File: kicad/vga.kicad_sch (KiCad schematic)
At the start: 19 parts, among them J2 DE15_Receptacle_HighDensity_M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, Q2 BC547, U17 74HC174, U18 XC9536PC44, U19 74HC574, U20 74HC574, U21 74HC245, U22 74HC02, U23 74HC138, U24 6264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

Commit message: Add user IO and USB
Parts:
- Q2: footprint Package_TO_SOT_THT_AKL:TO-92_Inline_Wide_CBE -> Package_TO_SOT_THT:TO-92
- U17: footprint Package_DIP:DIP-14_W7.62mm -> Package_DIP:DIP-16_W7.62mm
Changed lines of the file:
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@@
 			)
 		)
-		(property "Footprint" "Package_TO_SOT_THT_AKL:TO-92_Inline_Wide_CBE"
+		(property "Footprint" "Package_TO_SOT_THT:TO-92"
 			(at 270.51 88.9 0)
 			(effects
@@
 			)
 		)
-		(property "Footprint" "Package_DIP:DIP-14_W7.62mm"
+		(property "Footprint" "Package_DIP:DIP-16_W7.62mm"
 			(at 179.07 99.06 0)
 			(effects

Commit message: Add caps and make initial placement
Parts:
- added C26, C27, C28, C29, C30, C31, C32, C33, C34, C35, C36: 100n, Capacitor_THT:C_Disc_D5.0mm_W2.5mm_P2.50mm, symbol Device:C
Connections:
- net GND: now also C26.2, C27.2, C28.2, C29.2, C30.2, C31.2, C32.2, C33.2, C34.2, C35.2, C36.2
- net VCC: now also C26.1, C27.1, C28.1, C29.1, C30.1, C31.1, C32.1, C33.1, C34.1, C35.1, C36.1
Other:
- moved on the sheet: U22A

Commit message: Bugfixes, start routing
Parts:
- added U6: 74HC04, Package_DIP:DIP-14_W7.62mm, symbol 74xx:74HC04
- R15, R16, R17: value 330R -> 470R
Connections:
- net D6: no longer U20.8 (D6)
- net D7: no longer U19.9 (D7), U20.9 (D7)
- net GND: now also U19.9 (D7), U20.8 (D6), U20.9 (D7); no longer U22.2, U22.3, U23.6 (E2)
- net ROW3: now also U20.19 (Q0); no longer U19.12 (Q7)
- net ROW4: now also U20.18 (Q1); no longer U20.19 (Q0)
- net ROW5: now also U20.17 (Q2); no longer U20.18 (Q1)
- net ROW6: now also U20.16 (Q3); no longer U20.17 (Q2)
- net ROW7: now also U20.15 (Q4); no longer U20.16 (Q3)
- net ROW8: now also U20.14 (Q5); no longer U20.15 (Q4)
- net VCC: now also U23.6 (E2)
- net ~{BLANK}: now also U22.8; no longer U22.9
- net ~{WR}: now also U22.3; no longer U24.27 (~{WR})
- net at U22.11, U22.12: now also U19.1 (OE), U20.1 (OE), U21.19 (CE), U22.2, U23.15 (~{Y0}); no longer U24.22 (~{OE})
- net at U22.1: now also U24.22 (~{OE}), U6.13
- net at U27.13 (Qh): now also U22.9; no longer U22.8
- net at U20.13 (Q6): no longer U26.2 (A12)
- net ROMSEL0: now reaches U26.23 (A11)
- net ROMSEL0: no longer U20.14 (Q5)
- new net: U24.27 (~{WR}), U6.12
- new net ROMSEL1: U26.2 (A12)
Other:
- moved on the sheet: U22A, U22C

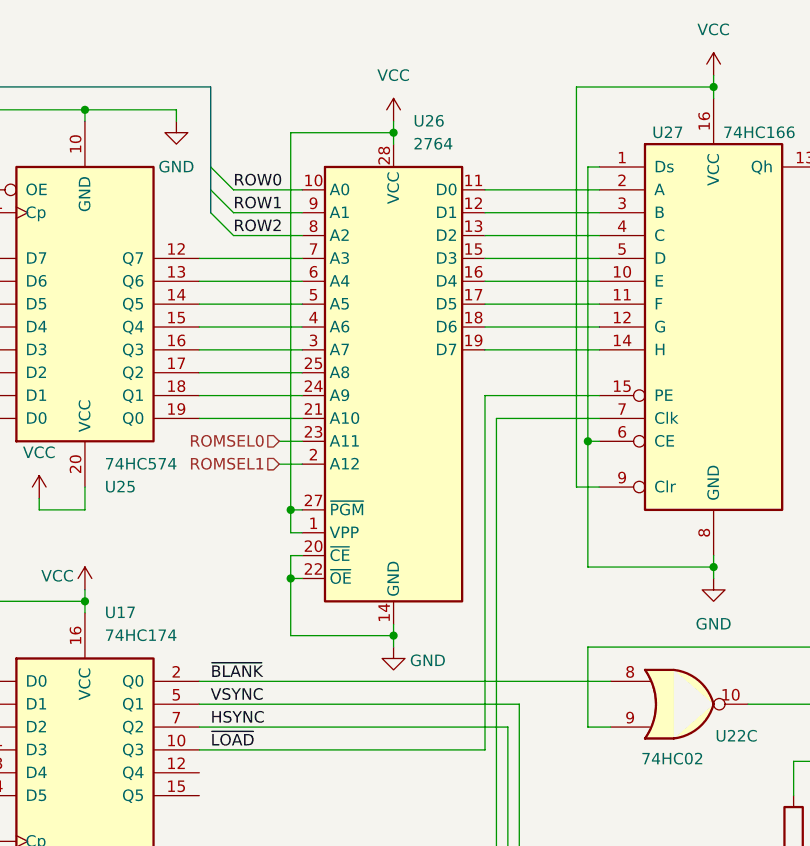
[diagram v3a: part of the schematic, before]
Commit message: Finished routing, HW prototype ready
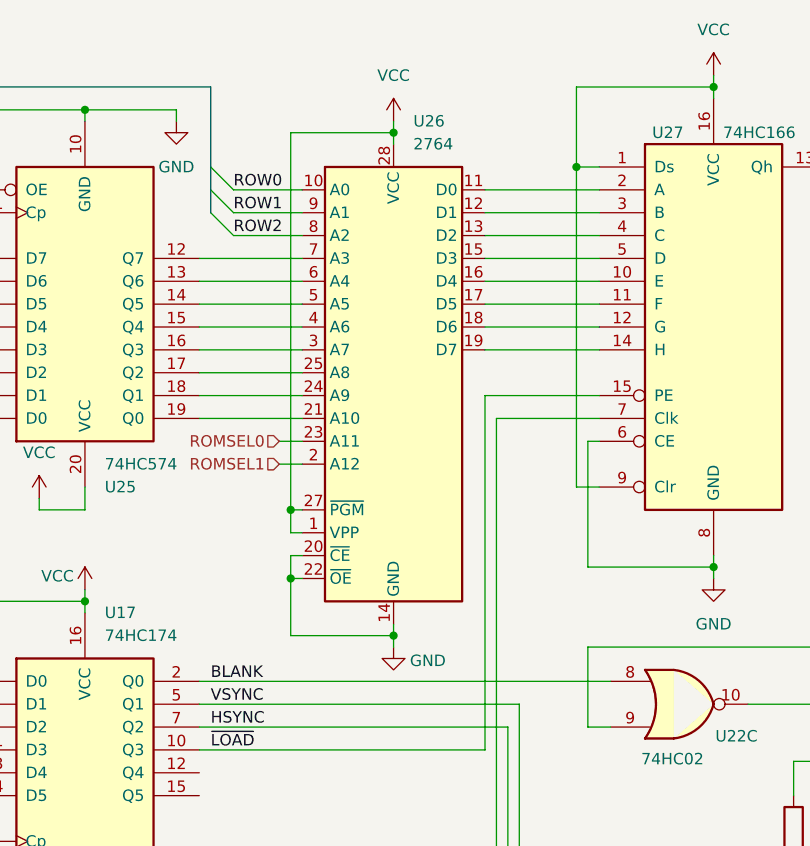
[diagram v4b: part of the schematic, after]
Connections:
- net GND: no longer U27.1 (Ds)
- net VCC: now also U27.1 (Ds)
- net ~{BLANK} renamed BLANK
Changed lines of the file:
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@@
 	)
 	(junction
+		(at 233.68 31.75)
+		(diameter 0)
+		(color 0 0 0 0)
+	)
+	(junction
 		(at 247.65 111.76)
 		(diameter 0)
@@
 	)
 	(junction
-		(at 234.95 62.23)
-		(diameter 0)
-		(color 0 0 0 0)
-	)
-	(junction
 		(at 163.83 125.73)
 		(diameter 0)
@@
 	(wire
 		(pts
-			(xy 233.68 22.86) (xy 233.68 67.31)
+			(xy 233.68 22.86) (xy 233.68 31.75)
 		)
 		(stroke
@@
 	(wire
 		(pts
+			(xy 233.68 31.75) (xy 233.68 67.31)
+		)
+		(stroke
+			(width 0)
+			(type default)
+		)
+	)
+	(wire
+		(pts
 			(xy 195.58 36.83) (xy 203.2 36.83)
 		)
@@
 	(wire
 		(pts
-			(xy 234.95 31.75) (xy 236.22 31.75)
+			(xy 233.68 31.75) (xy 236.22 31.75)
 		)
 		(stroke
@@
 	(wire
 		(pts
-			(xy 234.95 31.75) (xy 234.95 62.23)
-		)
-		(stroke
-			(width 0)
-			(type default)
-		)
-	)
-	(wire
-		(pts
 			(xy 71.12 144.78) (xy 74.93 144.78)
 		)
@@
 		)
 	)
-	(label "~{BLANK}"
+	(label "BLANK"
 		(at 193.04 88.9 0)
 		(fields_autoplaced yes)

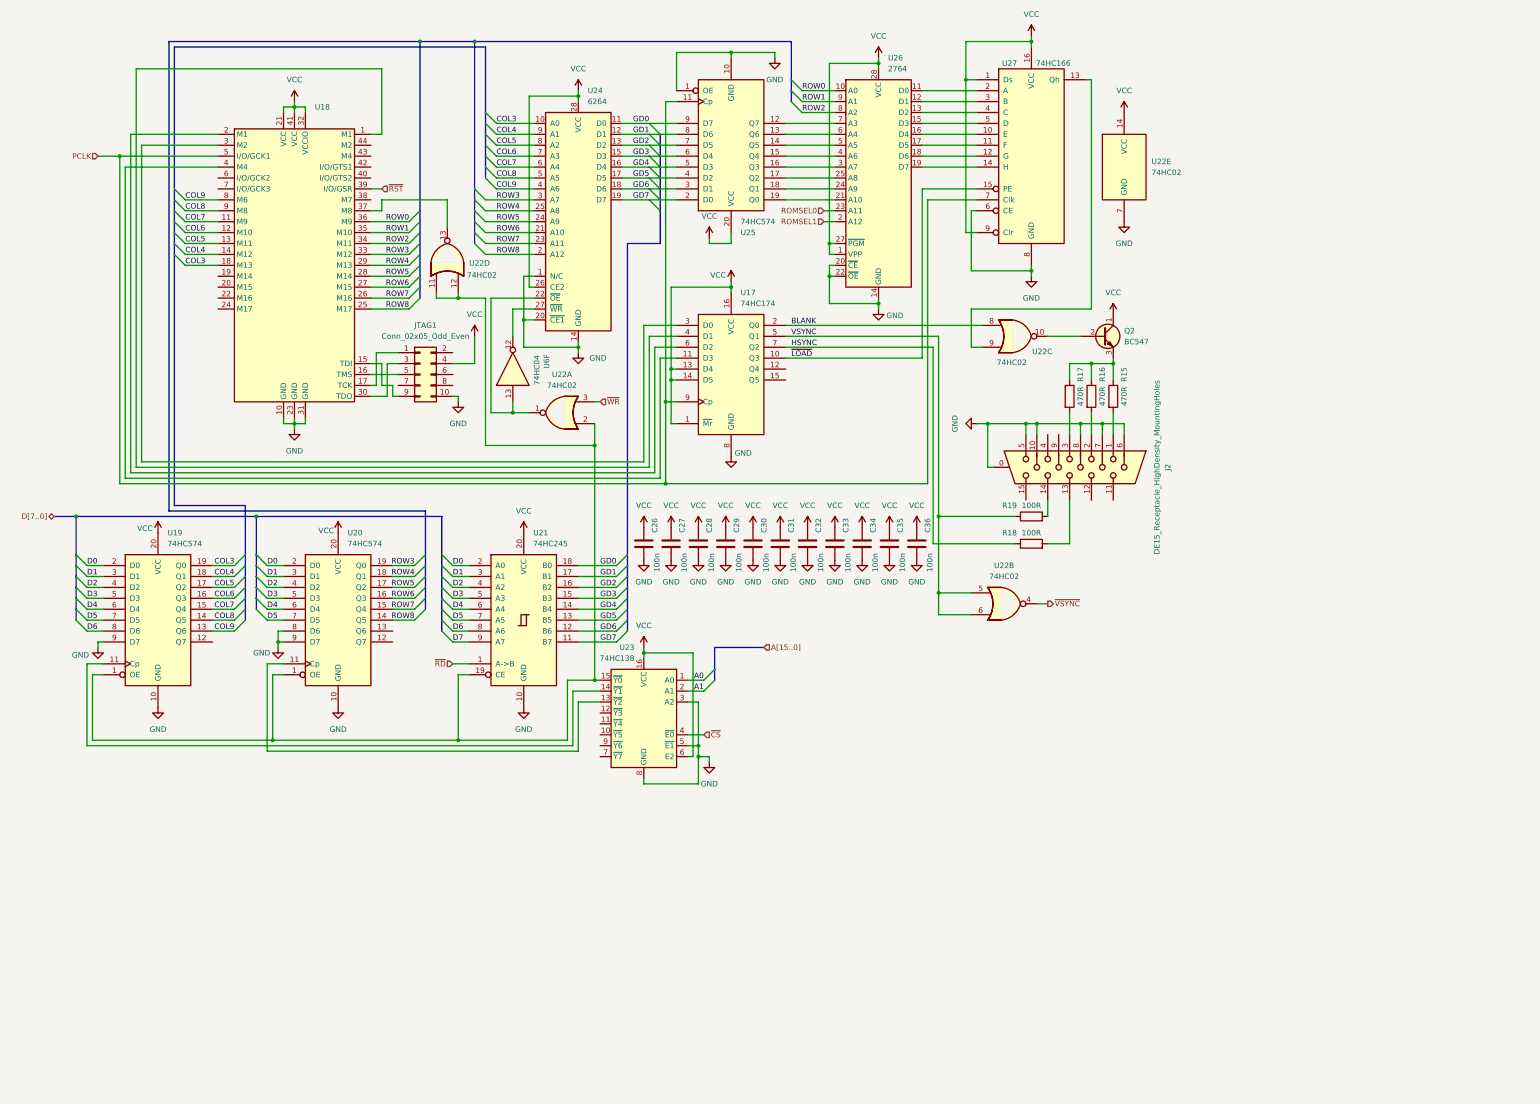
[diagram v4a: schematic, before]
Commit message: hw: Start work on rev B
Changelog:
- fixed IO address decoder (removed /PH2 gating),
- added missing reset circuit capacitor,
- added hardware VGA scrolling,
- removed VGA column register, replaced with address bus,
- fixed values of R5 and R6.
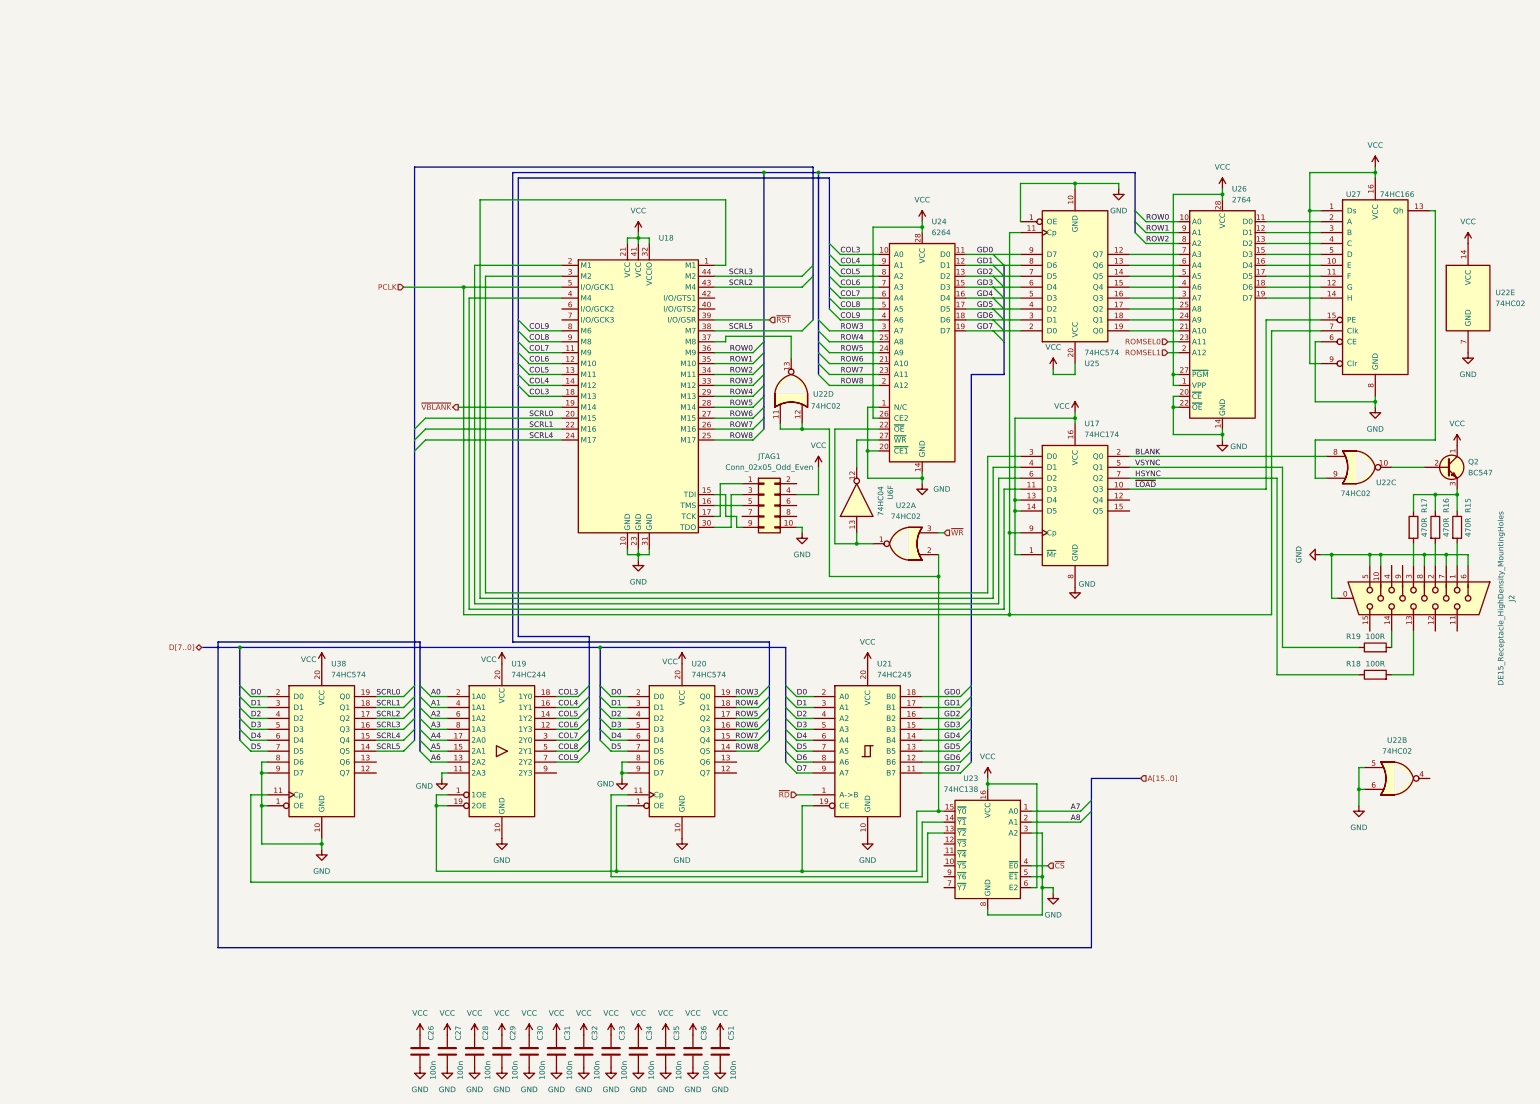
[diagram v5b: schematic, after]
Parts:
- removed U19: 74HC574, Package_DIP:DIP-20_W7.62mm, symbol 74xx:74HCT574
- added C51: 100n, Capacitor_THT:C_Disc_D5.0mm_W2.5mm_P2.50mm, symbol Device:C
- added U19: 74HC244, Package_DIP:DIP-20_W7.62mm, symbol 74xx:74HC244
- added U38: 74HC574, Package_DIP:DIP-20_W7.62mm, symbol 74xx:74HCT574
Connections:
- net A0: now also U19.2 (1A0); no longer U23.1 (A0)
- net A1: now also U19.4 (1A1); no longer U23.2 (A1)
- net COL3: now also U19.18 (1Y0)
- net COL4: now also U19.16 (1Y1)
- net COL5: now also U19.14 (1Y2)
- net COL6: now also U19.12 (1Y3)
- net COL7: now also U19.3 (2Y0)
- net COL8: now also U19.5 (2Y1)
- net COL9: now also U19.7 (2Y2)
- net D0: now also U38.2 (D0)
- net D1: now also U38.3 (D1)
- net D2: now also U38.4 (D2)
- net D3: now also U38.5 (D3)
- net D4: now also U38.6 (D4)
- net D5: now also U38.7 (D5)
- net GND: now also U22.5, U22.6, C51.2, U19.10 (GND), U19.11 (2A3), U38.1 (OE), U38.10 (GND), U38.8 (D6), U38.9 (D7)
- net VCC: now also C51.1, U19.20 (VCC), U38.20 (VCC)
- net VSYNC: no longer U22.5, U22.6
- net at U20.1 (OE), U21.19 (CE), U22.11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: now also U19.1 (1OE), U19.19 (2OE)
- net at U23.14 (~{Y1}): now also U20.11 (Cp)
- net at U23.13 (~{Y2}): now also U38.11 (Cp); no longer U20.11 (Cp)
- net ~{VBLANK}: now reaches U18.19 (M14)
- net SCRL0: now reaches U18.20 (M15)
- net SCRL0: now also U38.19 (Q0)
- net SCRL1: now reaches U18.22 (M16)
- net SCRL1: now also U38.18 (Q1)
- net SCRL4: now reaches U18.24 (M17)
- net SCRL4: now also U38.15 (Q4)
- net SCRL5: now reaches U18.38 (M7)
- net SCRL5: now also U38.14 (Q5)
- net SCRL2: now reaches U18.43 (M4)
- net SCRL2: now also U38.17 (Q2)
- net SCRL3: now reaches U18.44 (M2)
- net SCRL3: now also U38.16 (Q3)
- net ~{VSYNC}: no longer names the net of U22.4
- new net A2: U19.6 (1A2)
- new net A3: U19.8 (1A3)
- new net A4: U19.17 (2A0)
- new net A5: U19.15 (2A1)
- new net A6: U19.13 (2A2)
- new net A7: U23.1 (A0)
- new net A8: U23.2 (A1)
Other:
- moved on the sheet: C26, C27, C28, C29, C30, C31, C32, C33, C34, C35, C36, J2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

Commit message: hw: revision C
Major changes:
- ROM space has been extended from 16 KiB to 32 KiB
- dynamic RAM option has been removed
- RAM size has been reduced from 32 KiB to 24 KiB
- expansion slot now replaces internal ROM, does not
  have dedicated memory space anymore
- place all I/O within a compactish 8 KiB
- move PH2 gating to /RD and /WR signals
- PCB redo (mechanicaly compatible)
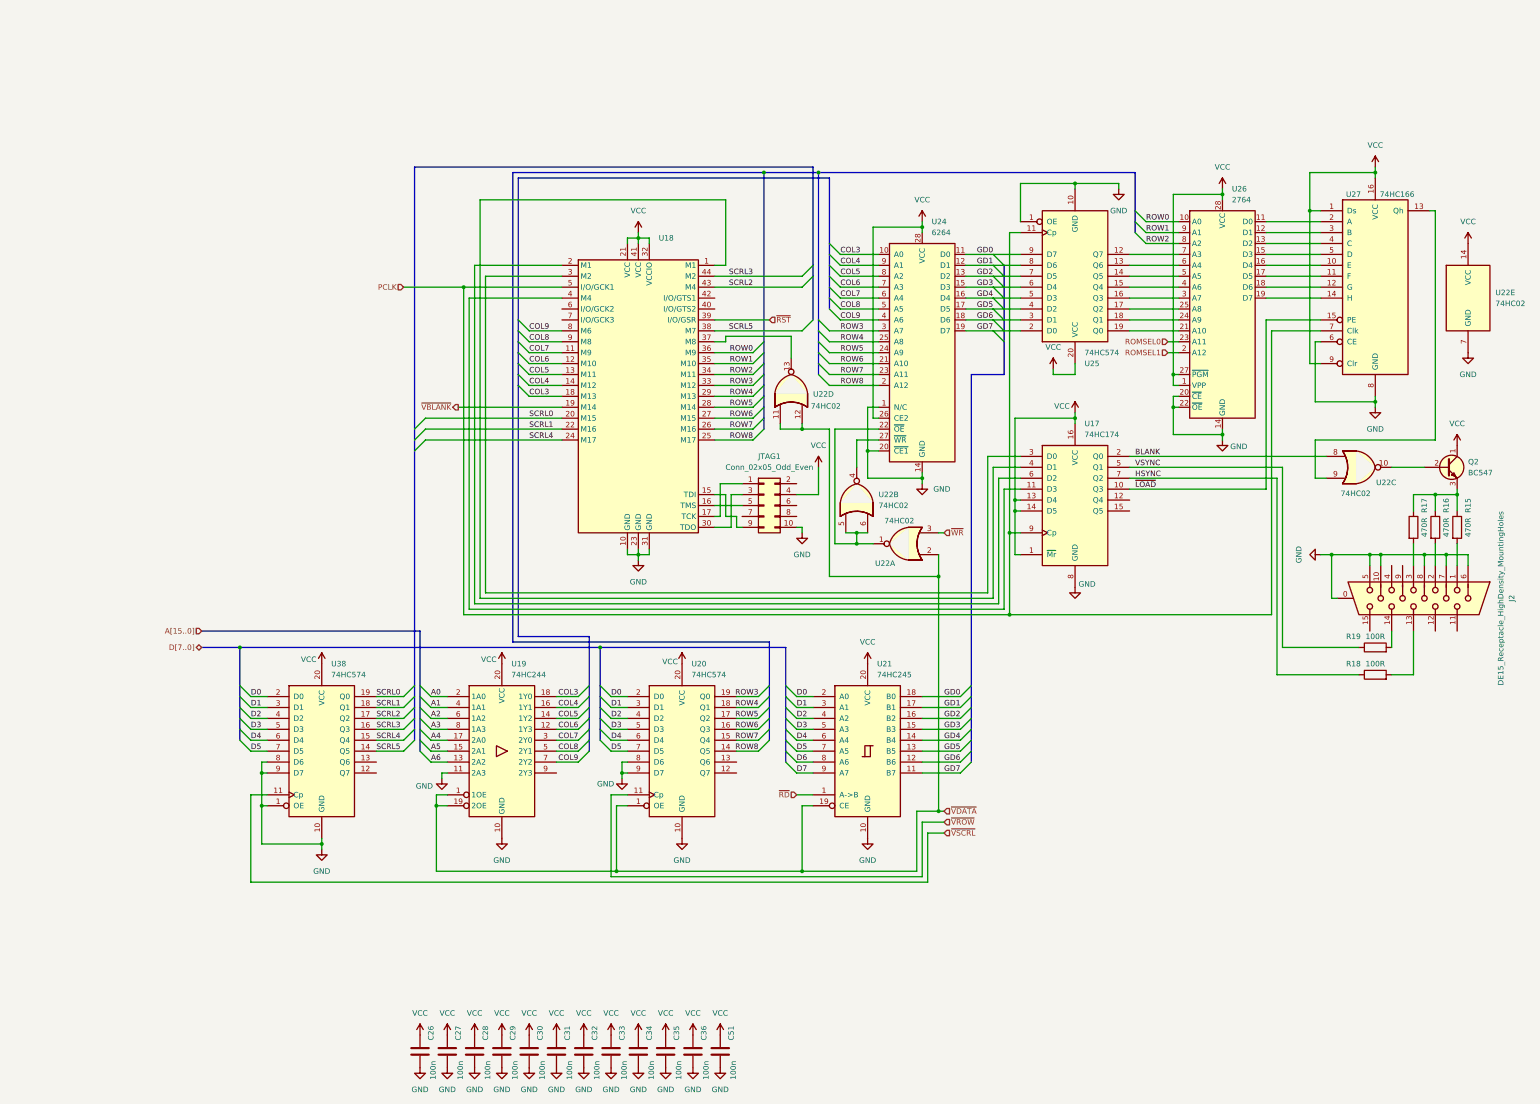
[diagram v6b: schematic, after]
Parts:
- removed U23: 74HC138, Package_DIP:DIP-16_W7.62mm, symbol 74xx:74HC138
- removed U6: 74HC04, Package_DIP:DIP-14_W7.62mm, symbol 74xx:74HC04
- U22: footprint PCM_Package_DIP_AKL:DIP-14_W7.62mm -> Package_DIP:DIP-14_W7.62mm
- U25: footprint PCM_Package_DIP_AKL:DIP-20_W7.62mm -> Package_DIP:DIP-20_W7.62mm
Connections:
- net GND: no longer U22.5, U22.6
- net at U22.4: now also U24.27 (~{WR})
- net ~{VDATA}: now reaches U19.1 (1OE), U19.19 (2OE), U20.1 (OE), U21.19 (CE), U22.11, U22.12, U22.2
- net ~{VSCRL}: now reaches U38.11 (Cp)
- net ~{VROW}: now reaches U20.11 (Cp)
- net at U22.1, U24.22 (~{OE}): now also U22.5, U22.6
